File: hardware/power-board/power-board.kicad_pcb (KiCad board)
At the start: 2 copper layers, 197 x 65 mm, 25 parts, among them J1 SW_SPST, J2 Main Board, J3 DMX512 Out Jack, J4 DMX512, K1 SPST-NO, K2 SPST-NO, P1 IEC320-C14, P2 IEC320-C13, P3 IEC320-C13, U1 NUD3112DMT1G, U2 MAX3075E

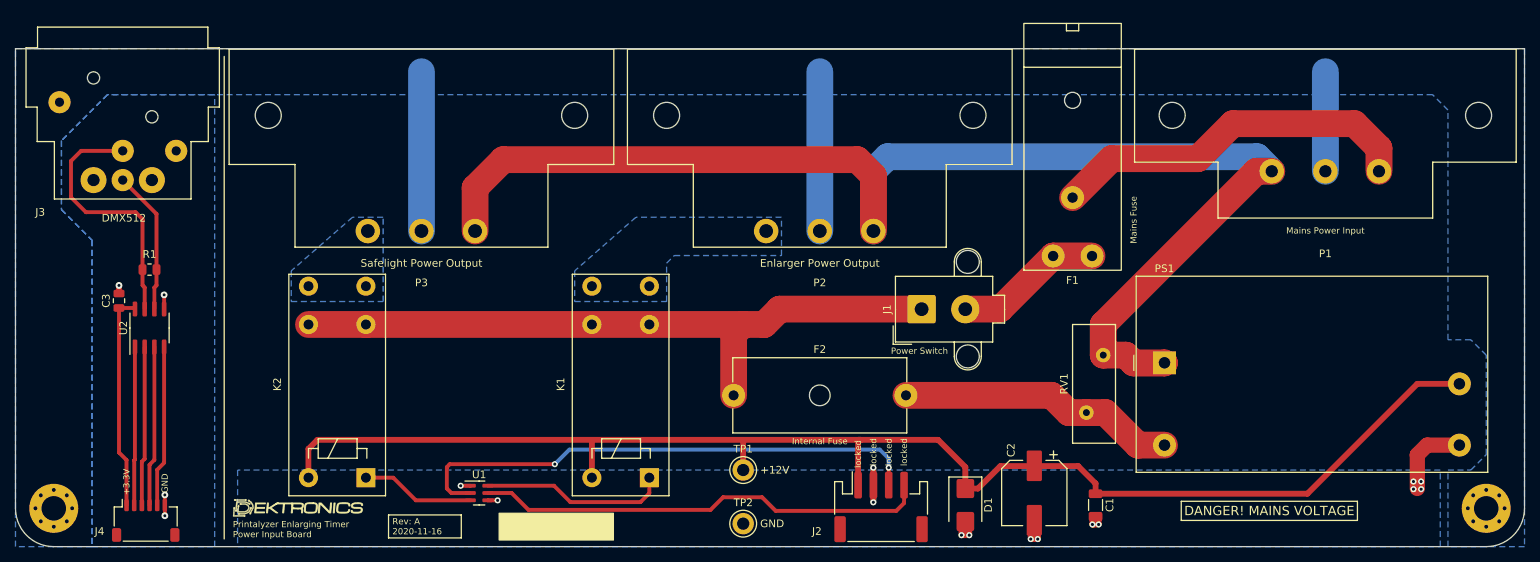
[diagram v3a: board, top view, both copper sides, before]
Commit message: Moved connectors to overhang board edge by 1mm
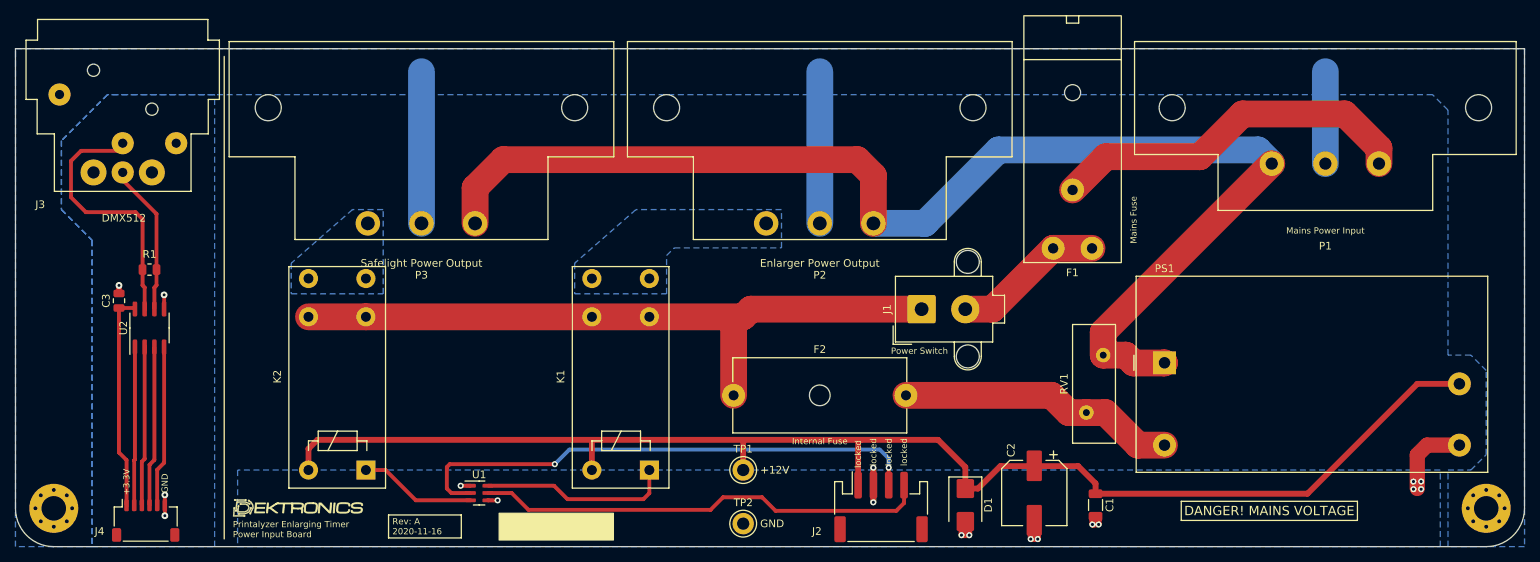
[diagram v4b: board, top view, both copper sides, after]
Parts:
- moved F1 1.00 mm to (173.0, 66.1)
- moved J3 1.00 mm to (45.2, 56.1)
- moved K1 1.00 mm to (110.2, 95.0)
- moved K2 1.00 mm to (73.2, 95.0)
- moved P1 1.00 mm to (206.0, 47.7)
- moved P2 1.00 mm to (140.0, 47.7)
- moved P3 1.00 mm to (88.0, 47.7)
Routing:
- net NEUT: track 171.4 -> 164.5 mm
- net Earth: track 54.6 -> 51.6 mm
- net +12V: track 183.2 -> 181.2 mm
- net LINE: track 90.6 -> 89.5 mm
- net Net-(U1-DRAIN1): track 24.5 -> 25.2 mm

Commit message: Swapped power switch connector and tweaked more power traces
Using a full receptacle and connector here takes up way too much space
and adds needless cost.  Going to instead try one of these spring
connectors that directly takes wires (with or without ferrules).
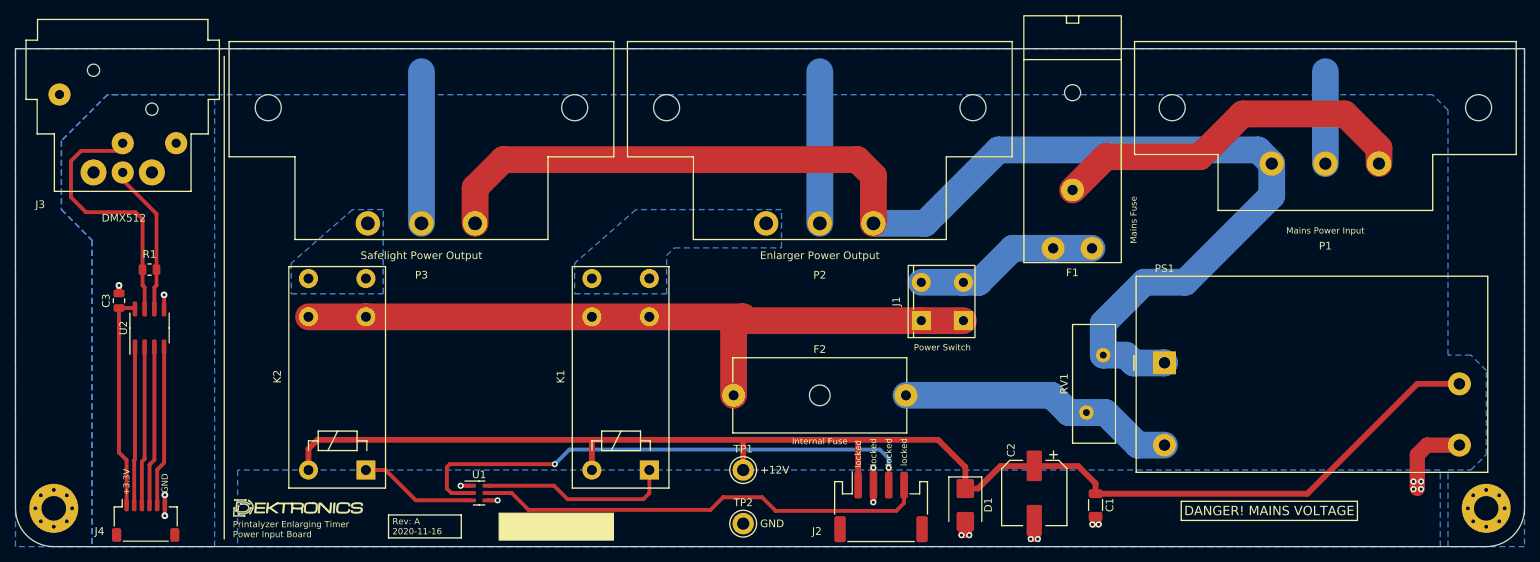
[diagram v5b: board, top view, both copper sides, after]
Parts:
- J1: footprint Connector_Molex:Molex_Mega-Fit_76829-0002_2x01_P5.70mm_Vertical -> lib_fp:Weidmuller_1825960000_1x02_P5.0mm
- moved J1 2.88 mm to (156.0, 73.0)
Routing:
- net LINE: track 89.5 -> 94.7 mm
- net Net-(J1-B): track 19.8 -> 24.1 mm
- net NEUT: track 164.5 -> 167.6 mm

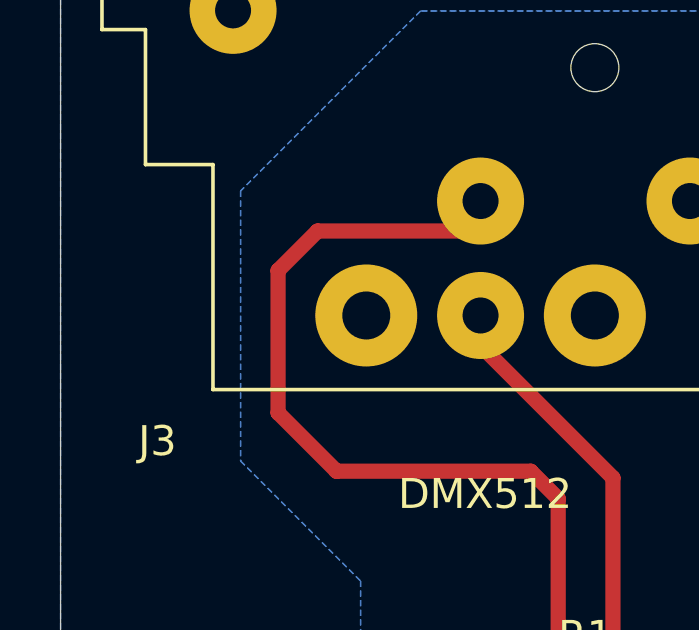
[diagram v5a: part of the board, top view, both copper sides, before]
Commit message: Added ground net tie for DMX512 port
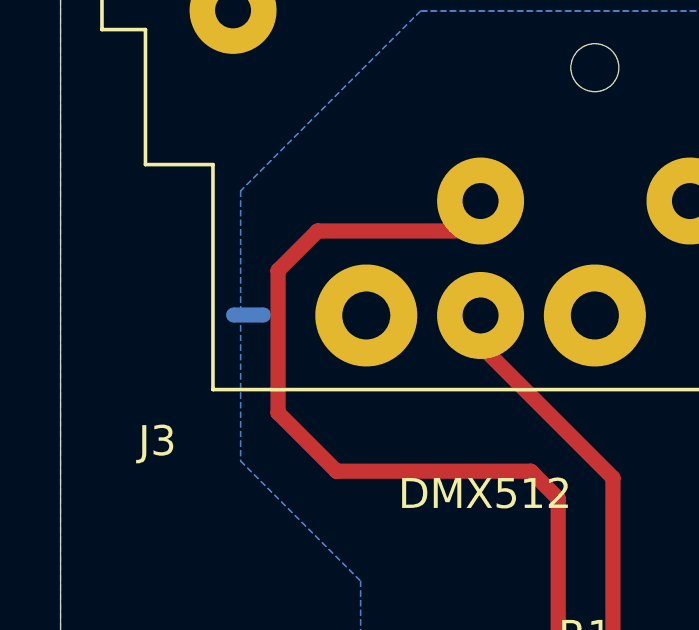
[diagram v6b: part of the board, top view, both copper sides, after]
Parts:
- added NT1: NetTie_2, NetTie:NetTie-2_SMD_Pad0.5mm, B.Cu at (41.3, 56.1)
- U1: value NUD3112DMT1G -> SZNUD3124DMT1G
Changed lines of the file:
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@@
     (property "Description" "IC PWR DRIVER N-CHANNEL 1:1 SC74")
     (property "Manufacturer" "ON Semiconductor")
-    (property "Manufacturer PN" "NUD3112DMT1G")
+    (property "Manufacturer PN" "SZNUD3124DMT1G")
     (property "Sheetfile" "power-board.kicad_sch")
     (property "Sheetname" "")
     (property "Supplier" "Digi-Key")
-    (property "Supplier PN" "NUD3112DMT1GOSCT-ND")
+    (property "Supplier PN" "SZNUD3124DMT1GOSCT-ND")
     (property "User Label" "Relay Driver")
     (property "ki_description" "2-Channel Parallel Integrated Relay, Inductive Load Driver, SC-74-6")
@@
         (effects (font (size 1 1) (thickness 0.15)))
     )
-    (fp_text value "NUD3112DMT1G" (at 0 2.4) (layer "F.Fab")
+    (fp_text value "SZNUD3124DMT1G" (at 0 2.4) (layer "F.Fab")
         (effects (font (size 1 1) (thickness 0.15)))
     )
@@
     )
   )
+  (footprint "NetTie:NetTie-2_SMD_Pad0.5mm" (layer "B.Cu")
+    (at 41.267 56.134 180)
+    (descr "Net tie, 2 pin, 0.5mm square SMD pads")
+    (tags "net tie")
+    (property "Description" "")
+    (property "Manufacturer" "")
+    (property "Manufacturer PN" "")
+    (property "Sheetfile" "power-board.kicad_sch")
+    (property "Sheetname" "")
+    (property "Supplier" "")
+    (property "Supplier PN" "")
+    (property "exclude_from_bom" "")
+    (property "ki_description" "Net tie, 2 pins")
+    (property "ki_keywords" "net tie short")
+    (zone_connect 2)
+    (attr exclude_from_pos_files exclude_from_bom)
+    (net_tie_pad_groups "1, 2")
+    (fp_text reference "NT1" (at 0 1.2) (layer "B.SilkS") hide
+        (effects (font (size 1 1) (thickness 0.15)) (justify mirror))
+    )
+    (fp_text value "NetTie_2" (at 0 -1.2) (layer "B.Fab") hide
+        (effects (font (size 1 1) (thickness 0.15)) (justify mirror))
+    )
+    (fp_poly
+      (pts
+        (xy -0.5 0.25)
+        (xy 0.5 0.25)
+        (xy 0.5 -0.25)
+        (xy -0.5 -0.25)
+      )
+      (stroke (width 0) (type solid)) (fill solid) (layer "B.Cu"))
+    (fp_line (start -1 -0.5) (end 1 -0.5)
+      (stroke (width 0.05) (type solid)) (layer "B.CrtYd"))
+    (fp_line (start -1 0.5) (end -1 -0.5)
+      (stroke (width 0.05) (type solid)) (layer "B.CrtYd"))
+    (fp_line (start 1 -0.5) (end 1 0.5)
+      (stroke (width 0.05) (type solid)) (layer "B.CrtYd"))
+    (fp_line (start 1 0.5) (end -1 0.5)
+      (stroke (width 0.05) (type solid)) (layer "B.CrtYd"))
+    (pad "1" smd circle (at -0.5 0 180) (size 0.5 0.5) (layers "B.Cu")
+      (net 17 "GND1") (pinfunction "1") (pintype "passive"))
+    (pad "2" smd circle (at 0.5 0 180) (size 0.5 0.5) (layers "B.Cu")
+      (net 9 "Earth") (pinfunction "2") (pintype "passive"))
+  )
   (gr_line locked (start 62.25 41) (end 62.25 104)

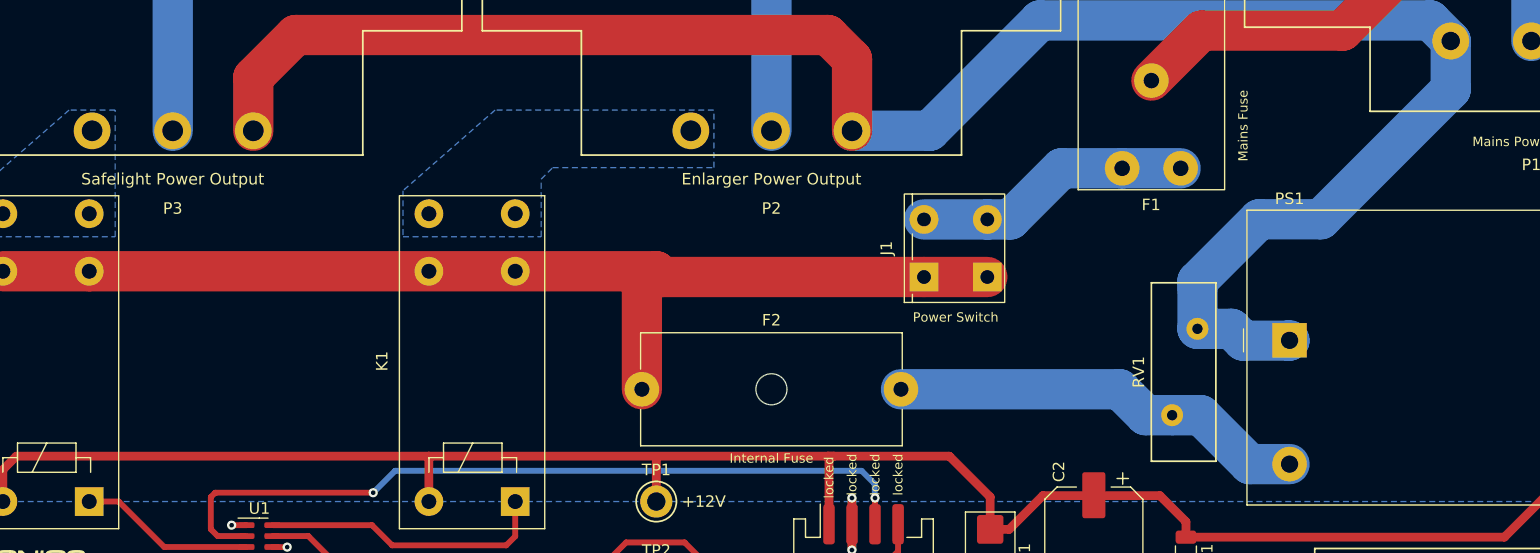
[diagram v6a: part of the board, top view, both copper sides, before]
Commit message: Move RV1 and F2 for better clearance from low voltage traces
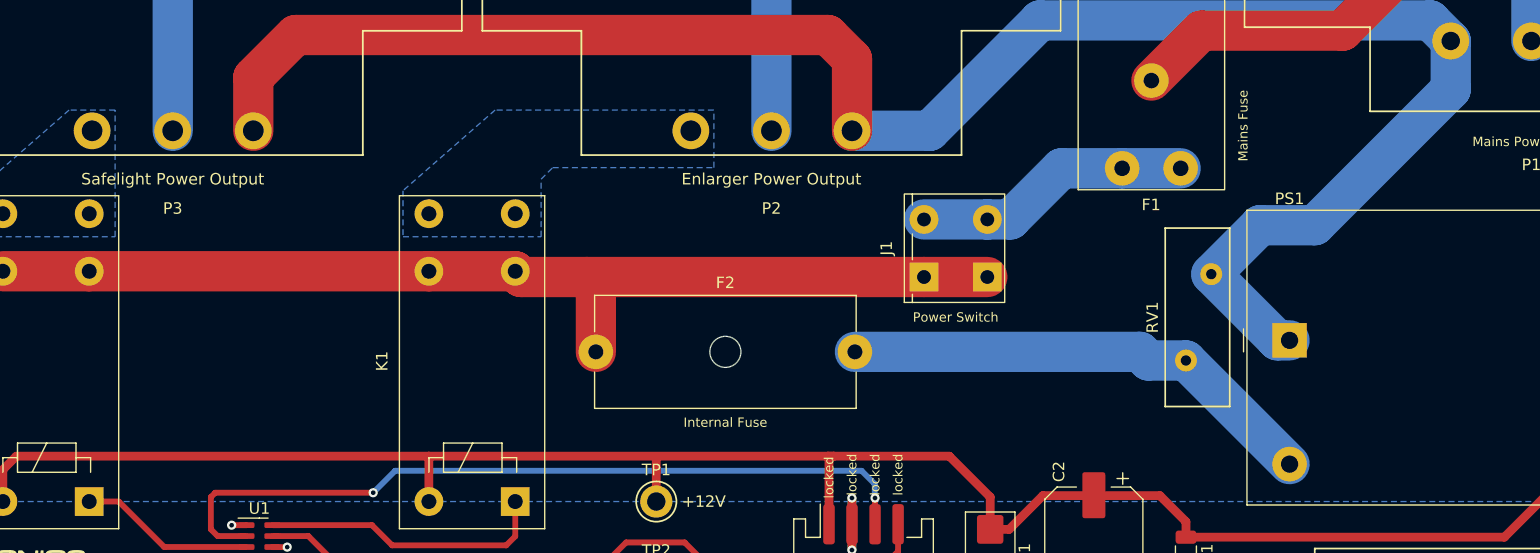
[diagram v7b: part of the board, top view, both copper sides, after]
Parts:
- moved F2 5.15 mm to (124.8, 82.0)
- moved RV1 4.90 mm to (178.2, 75.2)
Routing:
- net /AC_L: track 36.4 -> 41.8 mm
- net NEUT: track 167.6 -> 162.8 mm
- net LINE: track 94.7 -> 92.5 mm
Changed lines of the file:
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@@
   (net 23 "Net-(U1-DRAIN2)")
   (net 24 "Net-(P1-AC_L)")
-  (footprint "Fuse:Fuseholder_Cylinder-5x20mm_Schurter_0031_8201_Horizontal_Open" locked (layer "F.Cu")
-    (at 128.75 85.25)
+  (footprint "Fuse:Fuseholder_Cylinder-5x20mm_Schurter_0031_8201_Horizontal_Open" (layer "F.Cu")
+    (at 124.75 82)
     (descr "Fuseholder horizontal open, 5x20mm, 500V, 16A, Schurter 0031.8201, https://us.schurter.com/bundles/snceschurter/epim/_ProdPool_/newDS/en/typ_OGN.pdf")
     (tags "Fuseholder horizontal open 5x20 Schurter 0031.8201")
@@
     (fp_line (start 22.5 4.8) (end 22.5 -4.8)
       (stroke (width 0.1) (type solid)) (layer "F.Fab"))
-    (pad "" np_thru_hole circle locked (at 11.25 0) (size 2.7 2.7) (drill 2.7) (layers "*.Cu" "*.Mask"))
-    (pad "1" thru_hole circle locked (at 0 0) (size 3 3) (drill 1.3) (layers "*.Cu" "*.Mask")
+    (pad "" np_thru_hole circle (at 11.25 0) (size 2.7 2.7) (drill 2.7) (layers "*.Cu" "*.Mask"))
+    (pad "1" thru_hole circle (at 0 0) (size 3 3) (drill 1.3) (layers "*.Cu" "*.Mask")
       (net 3 "LINE") (pintype "passive"))
-    (pad "2" thru_hole circle locked (at 22.5 0) (size 3 3) (drill 1.3) (layers "*.Cu" "*.Mask")
+    (pad "2" thru_hole circle (at 22.5 0) (size 3 3) (drill 1.3) (layers "*.Cu" "*.Mask")
       (net 19 "/AC_L") (pintype "passive"))
     (model "${KICAD6_3DMODEL_DIR}/Fuse.3dshapes/Fuseholder_Cylinder-5x20mm_Schurter_0031_8201_Horizontal_Open.wrl"
@@
   )
   (footprint "lib_fp:RV_Disc_D15.5mm_W5.6mm_P7.5mm" (layer "F.Cu")
-    (at 177 80 -90)
+    (at 178.2 75.25 -90)
     (descr "Varistor, diameter 15.5mm, width 5.6mm, pitch 7.5mm (https://www.tdk-electronics.tdk.com/inf/70/db/var/SIOV_Leaded_StandarD.pdf)")
     (tags "varistor SIOV")
@@
     (effects (font (size 0.8128 0.8128) (thickness 0.1524)))
   )
-  (gr_text "Internal Fuse" (at 140 91.25) (layer "F.SilkS")
+  (gr_text "Internal Fuse" (at 136 88.138) (layer "F.SilkS")
     (effects (font (size 0.8128 0.8128) (thickness 0.1524)))
   )
@@
   (segment (start 167.962 94.488) (end 163.576 94.488) (width 0.762) (layer "F.Cu") (net 2))
   (segment (start 218.002 83.75) (end 203.659 98.093) (width 0.762) (layer "F.Cu") (net 2))
-  (segment (start 128.75 76.25) (end 128.75 85.25) (width 3.500001) (layer "F.Cu") (net 3))
+  (segment (start 124 75.5) (end 118.25 75.5) (width 3.500001) (layer "F.Cu") (net 3))
   (segment (start 153.25 75.5) (end 158.75 75.5) (width 3.500001) (layer "F.Cu") (net 3))
-  (segment (start 130 75) (end 80.75 75) (width 3.500001) (layer "F.Cu") (net 3))
+  (segment (start 110.25 75) (end 117.75 75) (width 3.500001) (layer "F.Cu") (net 3))
   (segment (start 80.75 75) (end 73.25 75) (width 3.500001) (layer "F.Cu") (net 3))
-  (segment (start 130.5 75.5) (end 153.25 75.5) (width 3.500001) (layer "F.Cu") (net 3))
-  (segment (start 130 75) (end 130.5 75.5) (width 3.500001) (layer "F.Cu") (net 3))
+  (segment (start 153.25 75.5) (end 124 75.5) (width 3.500001) (layer "F.Cu") (net 3))
+  (segment (start 124.75 82) (end 124.75 76.25) (width 3.500001) (layer "F.Cu") (net 3))
+  (segment (start 80.75 75) (end 110.25 75) (width 3.500001) (layer "F.Cu") (net 3))
+  (segment (start 124.75 76.25) (end 124 75.5) (width 3.500001) (layer "F.Cu") (net 3))
+  (segment (start 118.25 75.5) (end 117.75 75) (width 3.500001) (layer "F.Cu") (net 3))
   (segment (start 147 62.8) (end 147 56.576) (width 3.5) (layer "F.Cu") (net 6))
   (segment (start 144.907 54.483) (end 98.679 54.483) (width 3.5) (layer "F.Cu") (net 6))
@@
   (segment (start 147 56.576) (end 144.907 54.483) (width 3.5) (layer "F.Cu") (net 6))
   (segment (start 95 58.162) (end 95 62.8) (width 3.5) (layer "F.Cu") (net 6))
-  (segment (start 180.975 81.026) (end 184.974 81.026) (width 3.500001) (layer "B.Cu") (net 6))
   (segment (start 147 62.8) (end 153.735 62.8) (width 3.5) (layer "B.Cu") (net 6))
-  (segment (start 179.949 80) (end 180.975 81.026) (width 3.500001) (layer "B.Cu") (net 6))
-  (segment (start 184.974 81.026) (end 185 81) (width 3.500001) (layer "B.Cu") (net 6))
   (segment (start 153.735 62.8) (end 163.322 53.213) (width 3.5) (layer "B.Cu") (net 6))
   (segment (start 199 55) (end 199 59.191) (width 3.5) (layer "B.Cu") (net 6))
-  (segment (start 182.372 70.485) (end 177 75.857) (width 3.5) (layer "B.Cu") (net 6))
   (segment (start 197.213 53.213) (end 199 55) (width 3.5) (layer "B.Cu") (net 6))
+  (segment (start 187.191 71) (end 182.45 71) (width 3.5) (layer "B.Cu") (net 6))
   (segment (start 163.322 53.213) (end 197.213 53.213) (width 3.5) (layer "B.Cu") (net 6))
-  (segment (start 177 80) (end 179.949 80) (width 3.500001) (layer "B.Cu") (net 6))
-  (segment (start 187.706 70.485) (end 182.372 70.485) (width 3.5) (layer "B.Cu") (net 6))
-  (segment (start 177 75.857) (end 177 76.492) (width 3.5) (layer "B.Cu") (net 6))
-  (segment (start 199 59.191) (end 187.706 70.485) (width 3.5) (layer "B.Cu") (net 6))
-  (segment (start 177 80) (end 177 76.492) (width 3.500001) (layer "B.Cu") (net 6))
+  (segment (start 199 59.191) (end 187.191 71) (width 3.5) (layer "B.Cu") (net 6))
+  (segment (start 185 81) (end 183.95 81) (width 3.500001) (layer "B.Cu") (net 6))
+  (segment (start 183.95 81) (end 178.2 75.25) (width 3.500001) (layer "B.Cu") (net 6))
+  (segment (start 182.45 71) (end 178.2 75.25) (width 3.5) (layer "B.Cu") (net 6))
   (segment (start 91.313 94.615) (end 91.694 94.234) (width 0.508) (layer "F.Cu") (net 7))
   (segment (start 94.3925 98) (end 91.904 98) (width 0.508) (layer "F.Cu") (net 7))
@@
   (segment (start 165.19 66.06) (end 160.75 70.5) (width 3.500001) (layer "B.Cu") (net 18))
   (segment (start 160.75 70.5) (end 158.75 70.5) (width 3.500001) (layer "B.Cu") (net 18))
-  (segment (start 151.25 85.25) (end 170.25 85.25) (width 3.500001) (layer "B.Cu") (net 19))
-  (segment (start 170.25 85.25) (end 172.5 87.5) (width 3.500001) (layer "B.Cu") (net 19))
-  (segment (start 172.5 87.5) (end 174.8 87.5) (width 3.500001) (layer "B.Cu") (net 19))
-  (segment (start 181.539 91.75) (end 185 91.75) (width 3.500001) (layer "B.Cu") (net 19))
-  (segment (start 177.289 87.5) (end 181.539 91.75) (width 3.500001) (layer "B.Cu") (net 19))
-  (segment (start 174.8 87.5) (end 177.289 87.5) (width 3.500001) (layer "B.Cu") (net 19))
+  (segment (start 172.75 82.75) (end 176 82.75) (width 3.500001) (layer "B.Cu") (net 19))
+  (segment (start 172 82) (end 147.25 82) (width 3.500001) (layer "B.Cu") (net 19))
+  (segment (start 172.75 82.75) (end 172 82) (width 3.500001) (layer "B.Cu") (net 19))
+  (segment (start 185 91.75) (end 176 82.75) (width 3.500001) (layer "B.Cu") (net 19))
   (segment (start 105.305 97.05) (end 107.061 98.806) (width 0.508) (layer "F.Cu") (net 22))
   (segment (start 116.967 98.806) (end 117.75 98.023) (width 0.508) (layer "F.Cu") (net 22))
